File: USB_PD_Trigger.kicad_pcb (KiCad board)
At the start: 2 copper layers, 54.5 x 31.6 mm, 53 parts, among them J1 Conn_02x08_Odd_Even, J2 Conn_02x08_Odd_Even, J3 Conn_01x02, U1 AP33771C, U2 HP8KB7TB1, X1 2171790001, X2 Screw_Terminal_01x02

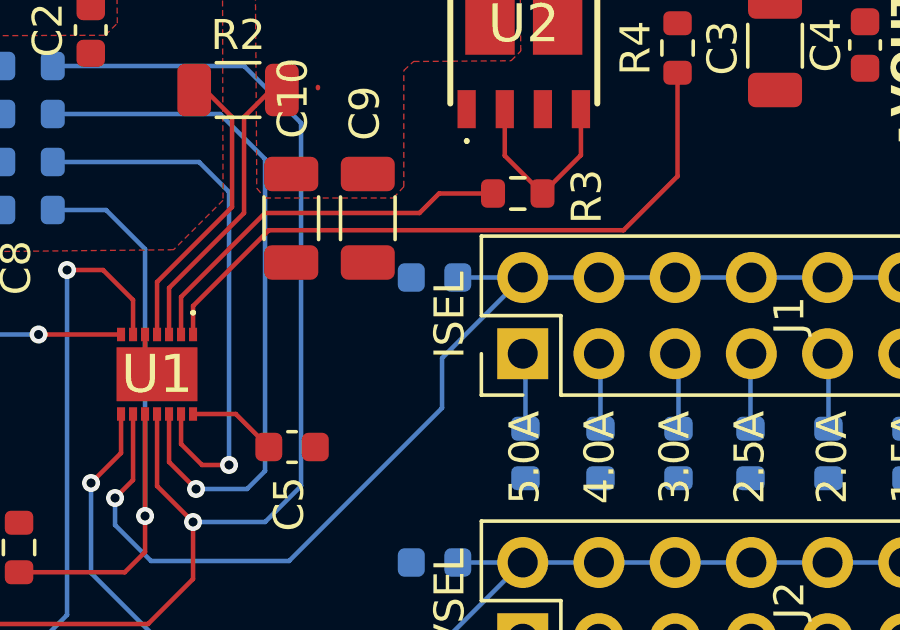
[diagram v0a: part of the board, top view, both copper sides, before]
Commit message: ISEL1 in Layout
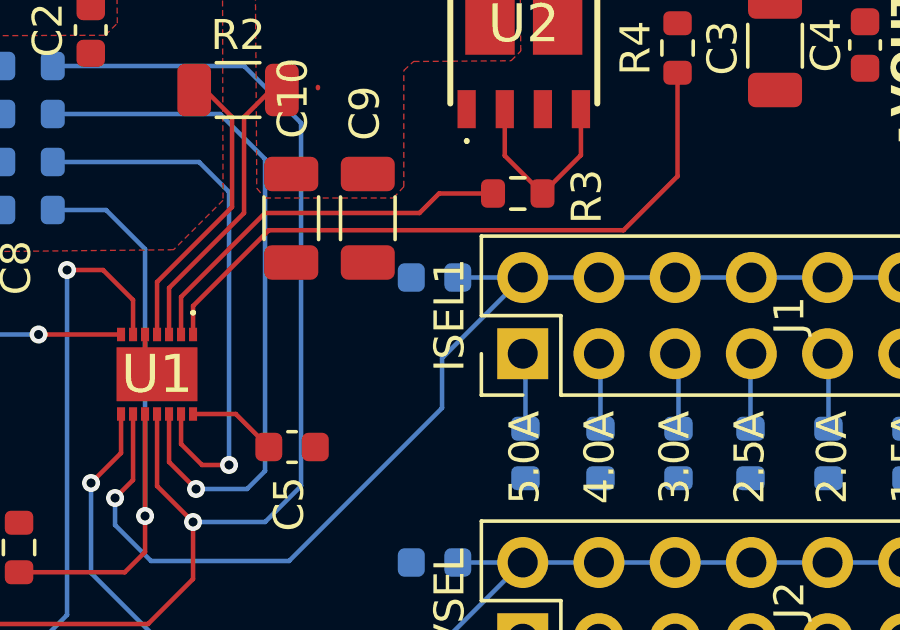
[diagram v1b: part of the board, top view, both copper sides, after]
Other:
- board text added: "ISEL1"
- board text removed: "ISEL"
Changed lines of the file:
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@@
 		)
 	)
-	(gr_text "ISEL"
+	(gr_text "ISEL1"
 		(at 102.25 86.5 90)
 		(layer "F.SilkS")

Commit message: ISEL in Layout
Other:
- board text added: "ISEL"
- board text removed: "ISEL1"
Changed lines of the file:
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@@
 		)
 	)
-	(gr_text "ISEL1"
+	(gr_text "ISEL"
 		(at 102.25 86.5 90)
 		(layer "F.SilkS")

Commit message: Zones completed
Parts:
- moved R4 55.4 mm to (159.7, 101.9)
- moved R5 54.5 mm to (177.1, 107.1)
- moved D2 54.3 mm to (176.9, 111.9)
- moved C10 54.1 mm to (147.0, 103.8)
- moved C3 54.1 mm to (163.1, 98.0)
- moved C4 54.1 mm to (166.1, 98.0)
- moved C5 54.1 mm to (147.0, 111.4)
- moved C6 54.1 mm to (151.8, 115.2)
- moved C7 54.1 mm to (151.8, 105.7)
- moved D1 54.1 mm to (128.3, 119.4)
- moved D3 54.1 mm to (131.5, 119.4)
- moved J1 54.1 mm to (154.7, 108.3)
- moved J2 54.1 mm to (154.7, 117.8)
- moved J3 54.1 mm to (128.6, 110.8)
- moved R1 54.1 mm to (128.3, 114.7)
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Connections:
- X1 pad : (no net) -> GND
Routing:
- net /VOUT: track 11.9 -> 0.00 mm
- net Net-(U1-VOUT): track 22.3 -> 18.5 mm
- added copper zone on F.Cu, net /VOUT
- added copper zone on B.Cu, net GND
- added copper zone on F.Cu, net GND
- added copper zone on F.Cu, net Net-(U2-S1)
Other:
- board size 54.5 x 31.6 mm -> 54.4 x 31.6 mm

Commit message: DRC errors resolution
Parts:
- added G***: LOGO, LOGO, F.Cu at (146.4, 118.1)
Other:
- board text added: "U1"
- board text added: "_electronic_projects"
- board text removed: "USB PD VOUT : 5V/9V/12V/15V/20V/28V"

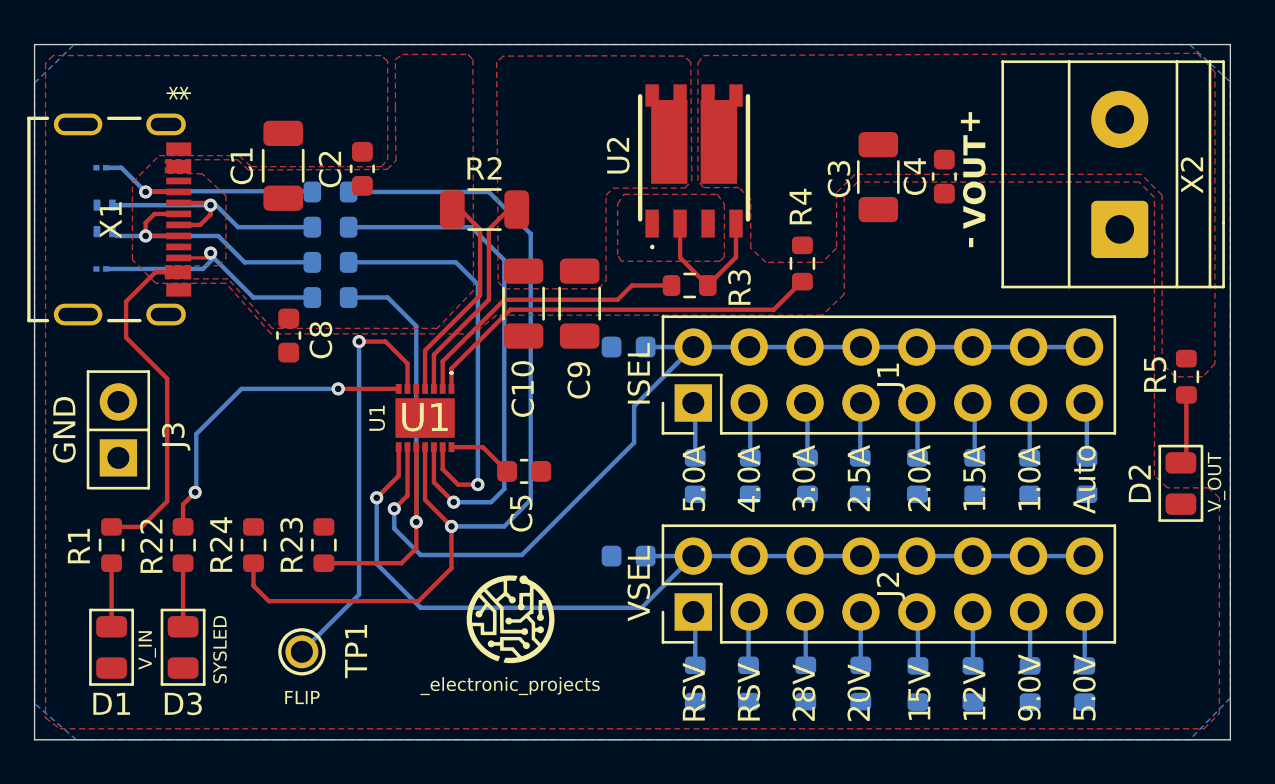
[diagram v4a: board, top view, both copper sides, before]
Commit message: DRC check complete + gerbers
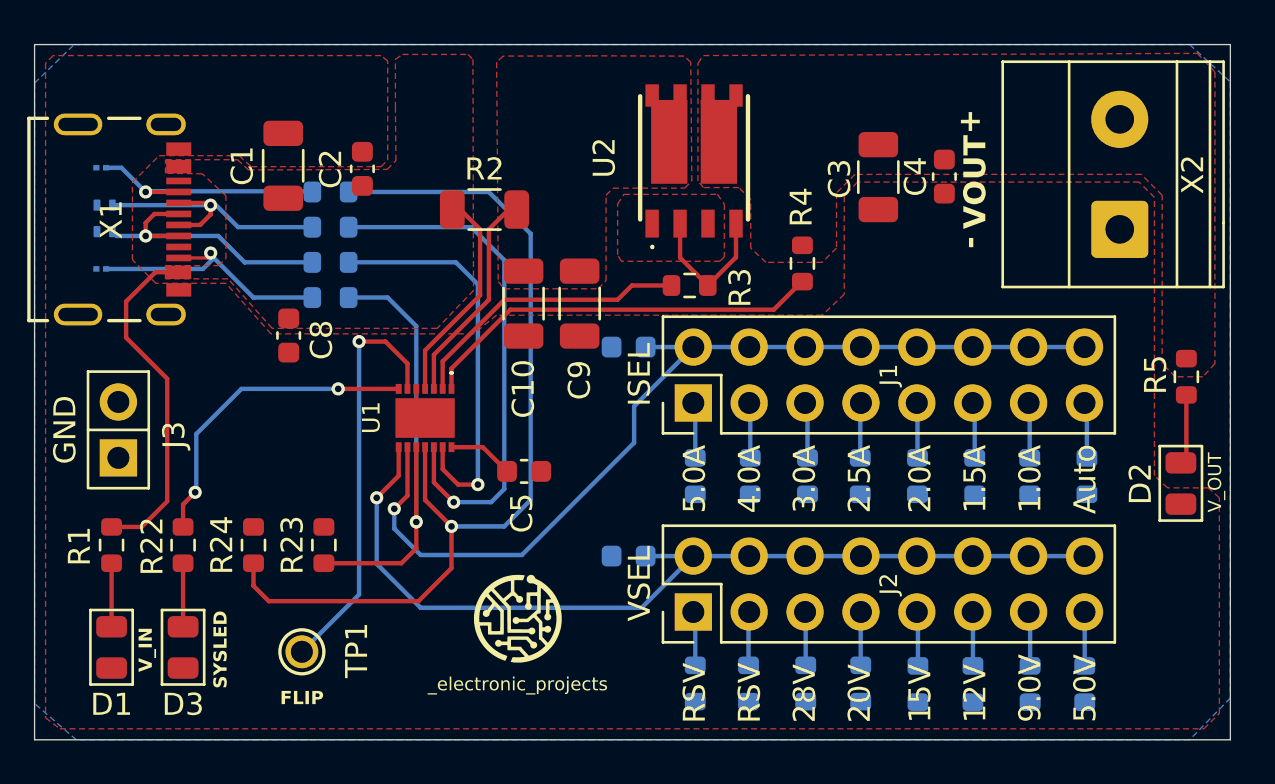
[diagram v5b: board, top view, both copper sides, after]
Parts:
- moved G*** 0.33 mm to (146.7, 118.1)
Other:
- board text removed: "U1"
